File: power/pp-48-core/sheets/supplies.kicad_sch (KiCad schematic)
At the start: 24 parts, among them J4 12V AUX OUT, U1 LM5164DDA, U2 URB4812YMD-6WR3

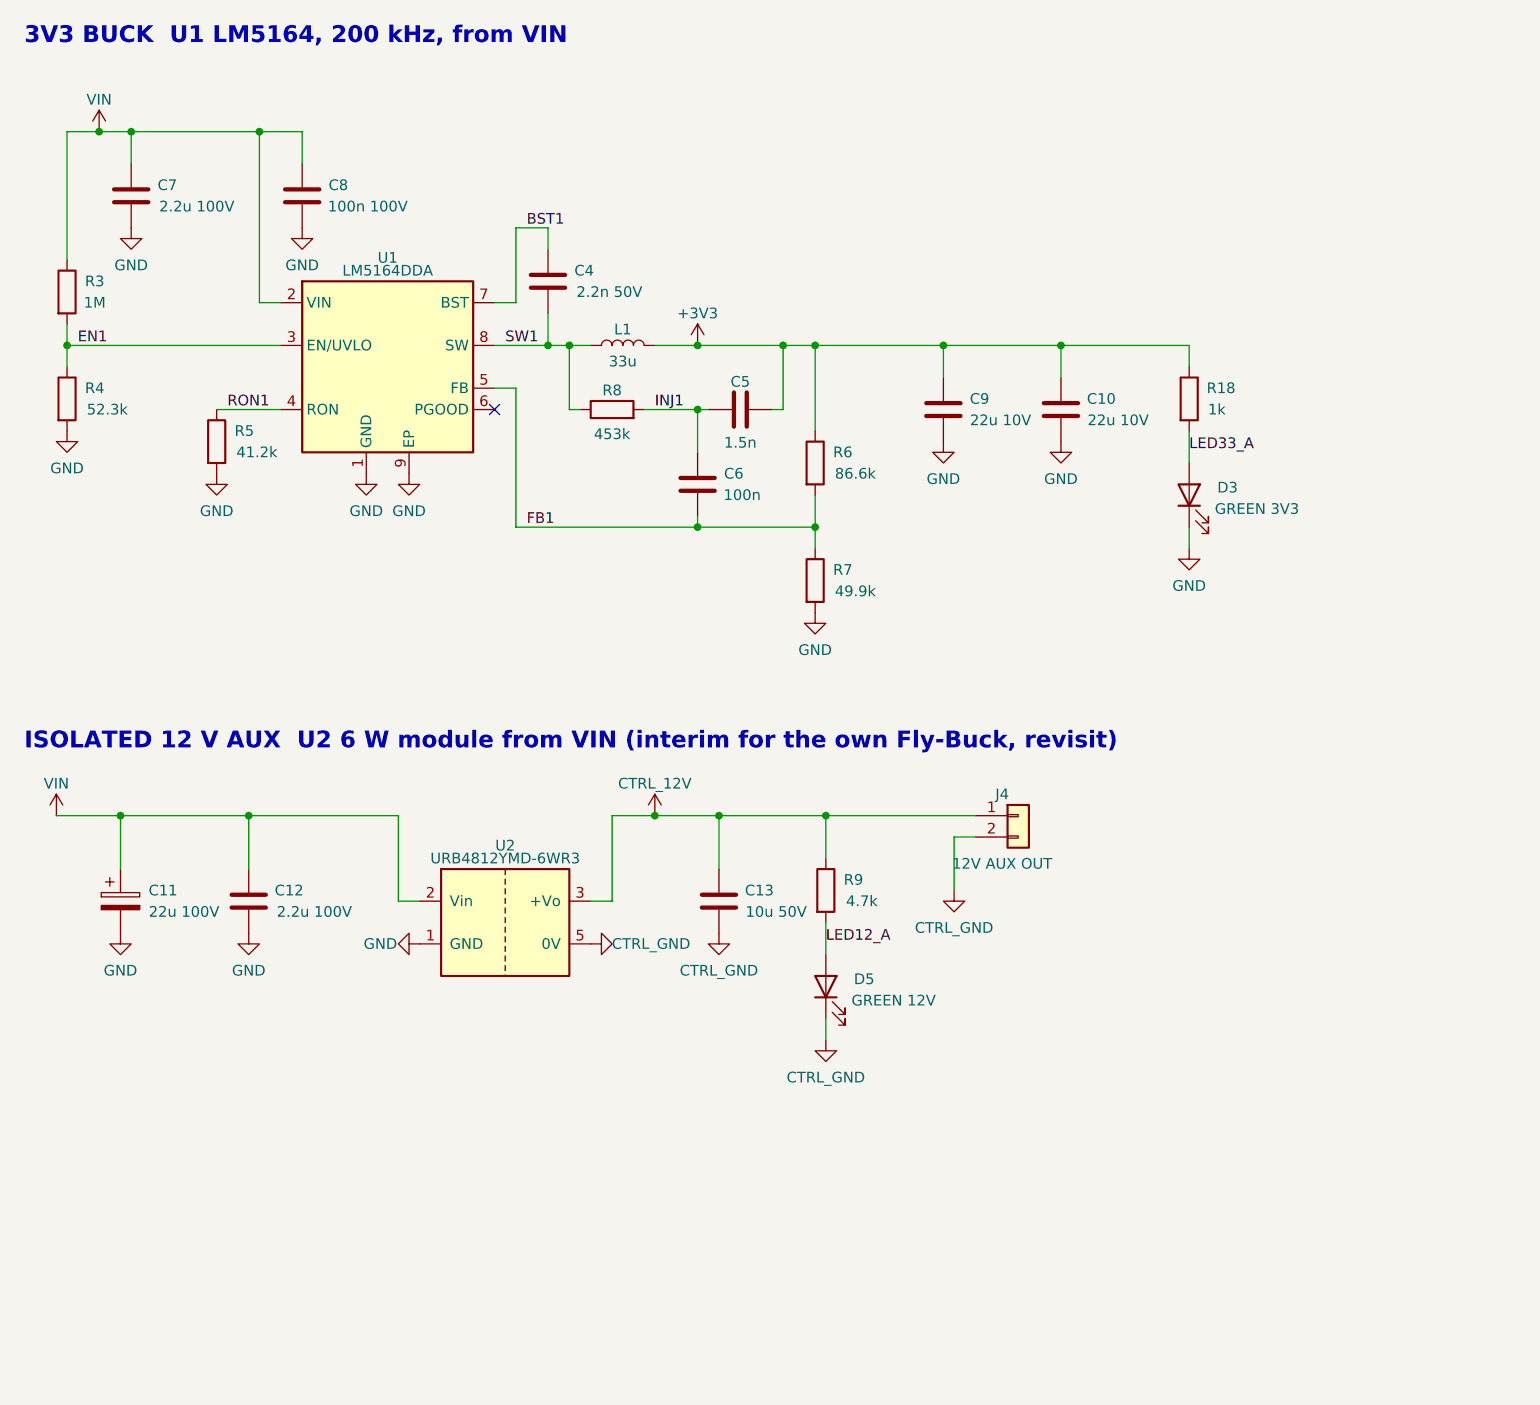
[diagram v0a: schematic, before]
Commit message: pp-48 core Supplies: LM5017 Fly-Buck replaces the interim 12 V module (ADR 0003 decision 14): L2 SRF0703-470M on the new footprint pp48:L_Bourns_SRF0703, secondary on the CTRL_GND island, PWR_FLAGs on CTRL_12V / CTRL_GND; ERC 0; handoff updated
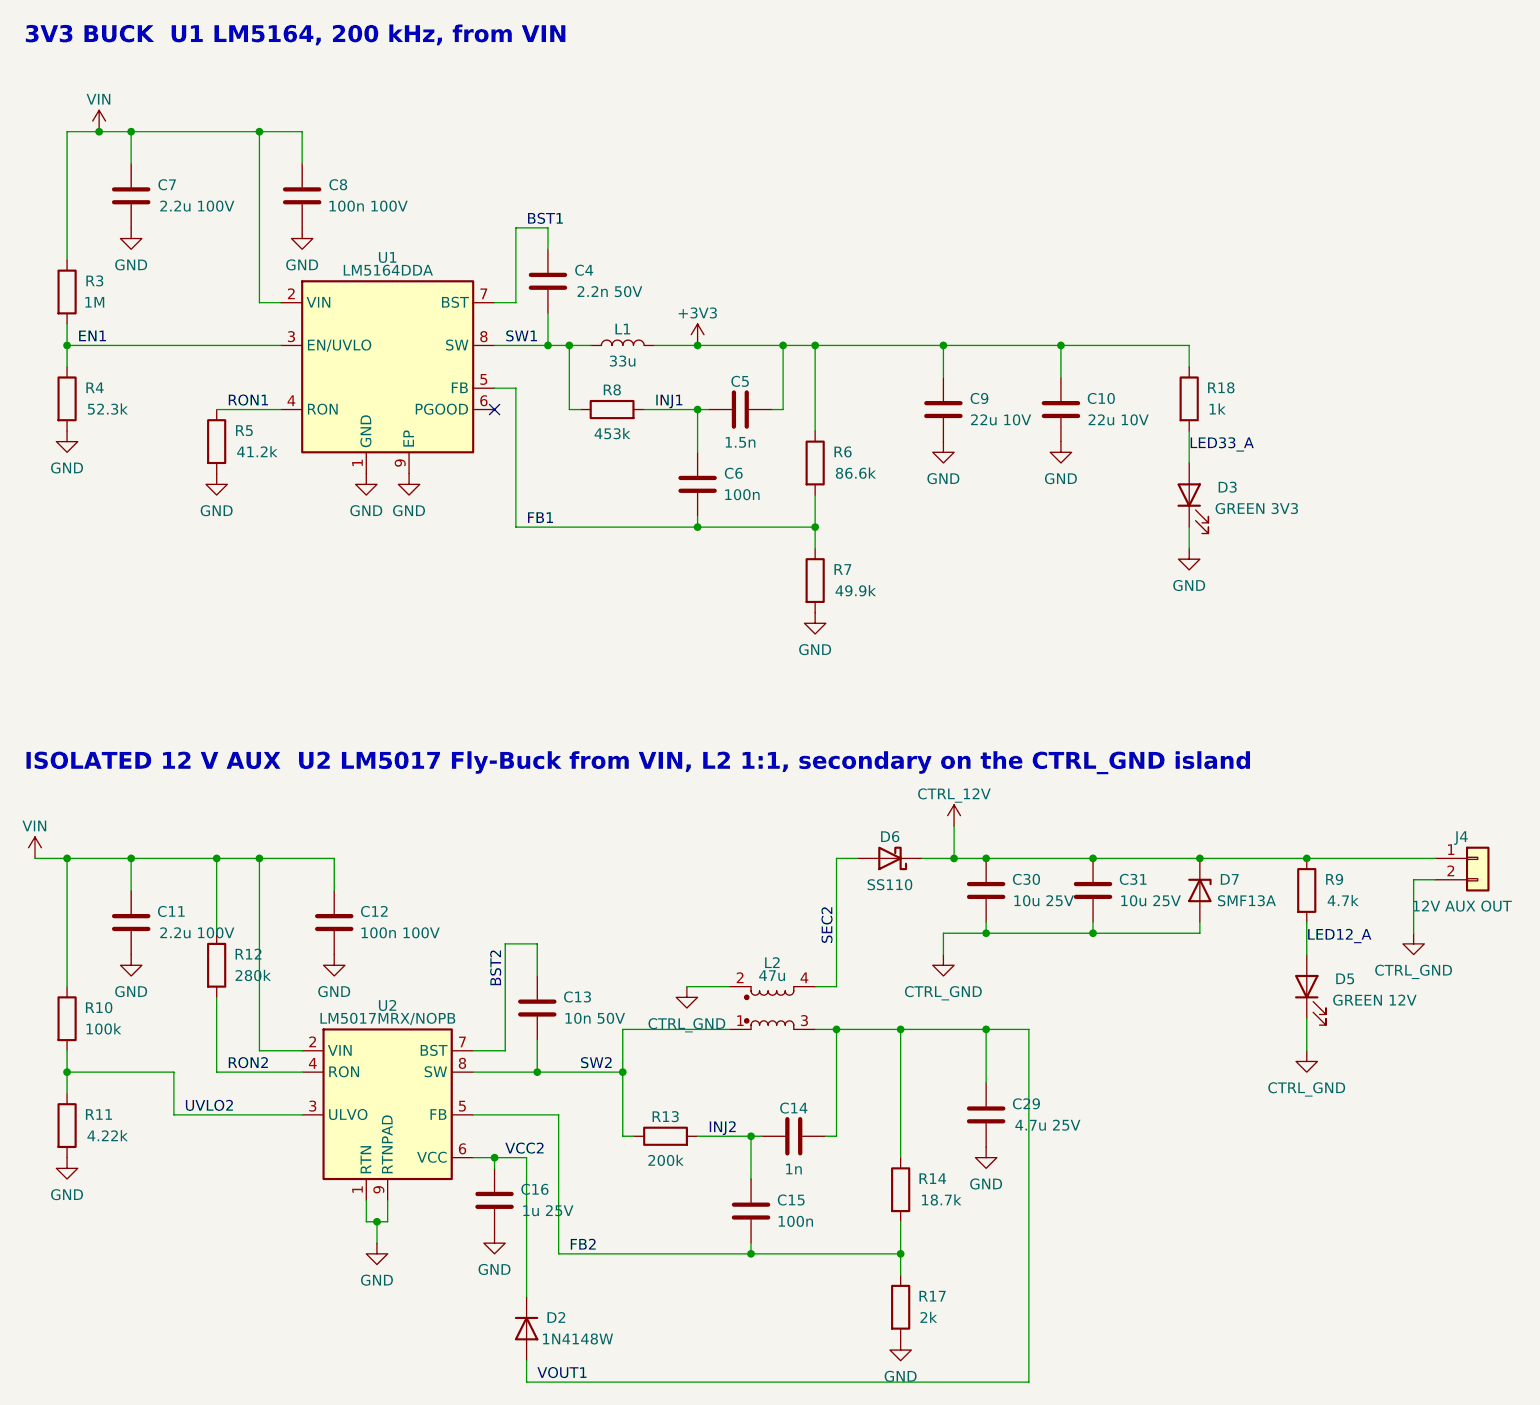
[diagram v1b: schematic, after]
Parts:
- added C14: 1n, Capacitor_SMD:C_0402_1005Metric, symbol Device:C
- added C15: 100n, Capacitor_SMD:C_0402_1005Metric, symbol Device:C
- added C16: 1u 25V, Capacitor_SMD:C_0603_1608Metric, symbol Device:C
- added C29: 4.7u 25V, Capacitor_SMD:C_0805_2012Metric, symbol Device:C
- added C30, C31: 10u 25V, Capacitor_SMD:C_0805_2012Metric, symbol Device:C
- added D2: 1N4148W, Diode_SMD:D_SOD-123, symbol Device:D
- added D6: SS110, Diode_SMD:D_SMA, symbol Device:D_Schottky
- added D7: SMF13A, Diode_SMD:D_SOD-123F, symbol Device:D_Zener
- added L2: 47u, pp48:L_Bourns_SRF0703, symbol Device:L_Coupled_1324
- added R10: 100k, Resistor_SMD:R_0805_2012Metric, symbol Device:R
- added R11: 4.22k, Resistor_SMD:R_0402_1005Metric, symbol Device:R
- added R12: 280k, Resistor_SMD:R_0805_2012Metric, symbol Device:R
- added R13: 200k, Resistor_SMD:R_0805_2012Metric, symbol Device:R
- added R14: 18.7k, Resistor_SMD:R_0402_1005Metric, symbol Device:R
- added R17: 2k, Resistor_SMD:R_0402_1005Metric, symbol Device:R
- C11: value 22u 100V -> 2.2u 100V; footprint Capacitor_SMD:CP_Elec_10x10 -> Capacitor_SMD:C_1210_3225Metric; symbol Device:C_Polarized -> Device:C; LCSC (none) -> C338133
- C12: value 2.2u 100V -> 100n 100V; footprint Capacitor_SMD:C_1210_3225Metric -> Capacitor_SMD:C_0603_1608Metric; LCSC C338133 -> (none)
- C13: value 10u 50V -> 10n 50V; footprint Capacitor_SMD:C_1210_3225Metric -> Capacitor_SMD:C_0402_1005Metric
- U2: value URB4812YMD-6WR3 -> LM5017MRX/NOPB; footprint pp48:Converter_DCDC_1x1in_THT -> Package_SO:SOIC-8-1EP_3.9x4.9mm_P1.27mm_EP2.95x4.9mm_Mask2.71x3.4mm_ThermalVias; symbol pp:DCDC_Iso_1x1_Single -> Regulator_Switching:LM5017MR; LCSC C5369743 -> C34355; MPN URB4812YMD-6WR3 (Mornsun pin-out; LCSC lists a YLPTEC part) -> (none)
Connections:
- net CTRL_12V: now also C30.1, C31.1, D6.1 (K), D7.1 (K); no longer C13.1, U2.3 (+Vo)
- net CTRL_GND: now also C30.2, C31.2, D7.2 (A), L2.2; no longer C13.2, U2.5 (0V)
- net GND: now also U2.9 (RTNPAD), C16.2, C29.2, R11.2, R17.2
- net VIN: now also R10.1, R12.1
- new net BST2: C13.1, U2.7 (BST)
- new net FB2: C15.2, R14.2, R17.1, U2.5 (FB)
- new net INJ2: C14.1, C15.1, R13.2
- new net RON2: R12.2, U2.4 (RON)
- new net SEC2: D6.2 (A), L2.4
- new net SW2: C13.2, L2.1, R13.1, U2.8 (SW)
- new net UVLO2: R10.2, R11.1, U2.3 (ULVO)
- new net VCC2: C16.1, D2.1 (K), U2.6 (VCC)
- new net VOUT1: C14.2, C29.1, D2.2 (A), L2.3, R14.1
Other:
- note added: "ISOLATED 12 V AUX U2 LM5017 Fly-Buck from VIN, L2 1:1, secondary on the CTRL_GND island"
- note removed: "ISOLATED 12 V AUX U2 6 W module from VIN (interim for the own Fly-Buck, revisit)"
- moved on the sheet: C12, C13, D5, J4, R9

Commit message: pp-48-core: GND stitch (1 via), silk (23 refs placed, 71 small ones hidden), JLC outputs; LCSC codes for the 25 passive values that had none (sch/draw.py BASIC table, JLC parts API: basic where JLC has one), copied onto the routed board; BOM 86 parts, left out only CV1/CV2, holes, J5 / JP1-3 (copper only) and DNP R28 / R29; DRC 0 unconnected, parity clean, isocheck clean
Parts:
- C10, C9: LCSC (none) -> C318780
- C12, C8: LCSC (none) -> C696916
- C13: LCSC (none) -> C15195
- C14: LCSC (none) -> C1523
- C16: LCSC (none) -> C15849
- C29: LCSC (none) -> C1779
- C30, C31: LCSC (none) -> C15850
- C4: LCSC (none) -> C1531
- C5: LCSC (none) -> C107022
- R10: LCSC (none) -> C149504
- R11: LCSC (none) -> C25898
- R12: LCSC (none) -> C5121536
- R13: LCSC (none) -> C17539
- R14: LCSC (none) -> C5153953
- R17: LCSC (none) -> C4109
- R3: LCSC (none) -> C17514
- R4: LCSC (none) -> C2998086
- R5: LCSC (none) -> C2998053
- R6: LCSC (none) -> C48533697
- R7: LCSC (none) -> C137969
- R8: LCSC (none) -> C27009
- R9: LCSC (none) -> C23162
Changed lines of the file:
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@@
 			)
 		)
-		(property "LCSC" ""
+		(property "LCSC" "C17514"
 			(at 19.05 46.99 0)
 			(hide yes)
@@
 			)
 		)
-		(property "LCSC" ""
+		(property "LCSC" "C2998086"
 			(at 19.05 59.69 0)
 			(hide yes)
@@
 			)
 		)
-		(property "LCSC" ""
+		(property "LCSC" "C2998053"
 			(at 36.83 64.77 0)
 			(hide yes)
@@
 			)
 		)
-		(property "LCSC" ""
+		(property "LCSC" "C696916"
 			(at 46.99 35.56 0)
 			(hide yes)
@@
 			)
 		)
-		(property "LCSC" ""
+		(property "LCSC" "C1531"
 			(at 76.2 45.72 0)
 			(hide yes)
@@
 			)
 		)
-		(property "LCSC" ""
+		(property "LCSC" "C27009"
 			(at 83.82 60.96 0)
 			(hide yes)
@@
 			)
 		)
-		(property "LCSC" ""
+		(property "LCSC" "C107022"
 			(at 99.06 60.96 0)
 			(hide yes)
@@
 			)
 		)
-		(property "LCSC" ""
+		(property "LCSC" "C48533697"
 			(at 107.95 67.31 0)
 			(hide yes)
@@
 			)
 		)
-		(property "LCSC" ""
+		(property "LCSC" "C137969"
 			(at 107.95 81.28 0)
 			(hide yes)
@@
 			)
 		)
-		(property "LCSC" ""
+		(property "LCSC" "C318780"
 			(at 123.19 60.96 0)
 			(hide yes)
@@
 			)
 		)
-		(property "LCSC" ""
+		(property "LCSC" "C318780"
 			(at 137.16 60.96 0)
 			(hide yes)
@@
 			)
 		)
-		(property "LCSC" ""
+		(property "LCSC" "C149504"
 			(at 19.05 133.35 0)
 			(hide yes)
@@
 			)
 		)
-		(property "LCSC" ""
+		(property "LCSC" "C25898"
 			(at 19.05 146.05 0)
 			(hide yes)
@@
 			)
 		)
-		(property "LCSC" ""
+		(property "LCSC" "C5121536"
 			(at 36.83 127 0)
 			(hide yes)
@@
 			)
 		)
-		(property "LCSC" ""
+		(property "LCSC" "C696916"
 			(at 50.8 121.92 0)
 			(hide yes)
@@
 			)
 		)
-		(property "LCSC" ""
+		(property "LCSC" "C15195"
 			(at 74.93 132.08 0)
 			(hide yes)
@@
 			)
 		)
-		(property "LCSC" ""
+		(property "LCSC" "C17539"
 			(at 90.17 147.32 0)
 			(hide yes)
@@
 			)
 		)
-		(property "LCSC" ""
+		(property "LCSC" "C1523"
 			(at 105.41 147.32 0)
 			(hide yes)
@@
 			)
 		)
-		(property "LCSC" ""
+		(property "LCSC" "C5153953"
 			(at 118.11 153.67 0)
 			(hide yes)
@@
 			)
 		)
-		(property "LCSC" ""
+		(property "LCSC" "C4109"
 			(at 118.11 167.64 0)
 			(hide yes)
@@
 			)
 		)
-		(property "LCSC" ""
+		(property "LCSC" "C15849"
 			(at 69.85 154.94 0)
 			(hide yes)
@@
 			)
 		)
-		(property "LCSC" ""
+		(property "LCSC" "C1779"
 			(at 128.27 144.78 0)
 			(hide yes)
@@
 			)
 		)
-		(property "LCSC" ""
+		(property "LCSC" "C15850"
 			(at 128.27 118.11 0)
 			(hide yes)
@@
 			)
 		)
-		(property "LCSC" ""
+		(property "LCSC" "C15850"
 			(at 140.97 118.11 0)
 			(hide yes)
@@
 			)
 		)
-		(property "LCSC" ""
+		(property "LCSC" "C23162"
 			(at 166.37 118.11 0)
 			(hide yes)

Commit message: pp-48-core 12 V aux: LM5018 + Coilcraft LPD5030V-333 replace the LM5017 + SRF0703 (ADR 0003 decision 14 revised): the SRF0703's real land pattern puts its windings' pads 0.46 mm apart with no isolation rating; the LPD5030V (4.8 x 4.8 mm, 1000 V winding to winding) has one winding per side, so the island barrier is straight (1.48 mm under the part), no pocket or vias; ~1.2 W, RON 169k (~800 kHz); footprint pp48:L_Coilcraft_LPD5030V from Coilcraft's land pattern with the LCSC 3D model; re-placed, routed, U2 exposed pad solid, gnd stitch, silk, JLC outputs. 3D models: L1 on Inductor_SMD:L_Bourns_SRR1260 (the part, SRR1260-330M; pads 0.1 mm further in than the generic 12x12, stock model), U2 on a project copy of its SOIC-8-1EP footprint pointing at the stock EP2.41x3.81 STEP (the referenced one is not shipped); both swapped on the routed board in place. ERC 0, DRC 0 unconnected, parity clean, isocheck clean, BOM 86 parts; handoff
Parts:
- L1: footprint Inductor_SMD:L_12x12mm_H6mm -> Inductor_SMD:L_Bourns_SRR1260
- L2: value 47u -> 33u; footprint pp48:L_Bourns_SRF0703 -> pp48:L_Coilcraft_LPD5030V; symbol Device:L_Coupled_1324 -> Device:L_Coupled_1243; LCSC C3273458 -> C5441621; MPN Bourns SRF0703-470M -> Coilcraft LPD5030V-333MRC
- R12: value 280k -> 169k; LCSC C5121536 -> C2933337
- U2: value LM5017MRX/NOPB -> LM5018MRX/NOPB; footprint Package_SO:SOIC-8-1EP_3.9x4.9mm_P1.27mm_EP2.95x4.9mm_Mask2.71x3.4mm_ThermalVias -> pp48:SOIC-8-1EP_3.9x4.9mm_P1.27mm_EP2.95x4.9mm_Mask2.71x3.4mm_ThermalVias; LCSC C34355 -> C471040
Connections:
- net CTRL_GND: now also L2.4; no longer L2.2
- net SEC2: now also L2.3; no longer L2.4
- net VOUT1: now also L2.2; no longer L2.3
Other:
- note added: "ISOLATED 12 V AUX U2 LM5018 Fly-Buck from VIN, L2 1:1, secondary on the CTRL_GND island"
- note removed: "ISOLATED 12 V AUX U2 LM5017 Fly-Buck from VIN, L2 1:1, secondary on the CTRL_GND island"
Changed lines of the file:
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@@
 		)
 	)
-	(text "ISOLATED 12 V AUX  U2 LM5017 Fly-Buck from VIN, L2 1:1, secondary on the CTRL_GND island"
+	(text "ISOLATED 12 V AUX  U2 LM5018 Fly-Buck from VIN, L2 1:1, secondary on the CTRL_GND island"
 		(exclude_from_sim no)
 		(at 13.97 104.14 0)
@@
 			)
 		)
-		(property "Footprint" "Inductor_SMD:L_12x12mm_H6mm"
+		(property "Footprint" "Inductor_SMD:L_Bourns_SRR1260"
 			(at 85.09 53.34 0)
 			(hide yes)
@@
 			)
 		)
-		(property "Description" "shielded, Isat >= 1.5 A, 12x12 land pattern (SRR1260 / CDRH127 class)"
+		(property "Description" "shielded, Isat >= 1.5 A, Bourns SRR1260 land pattern"
 			(at 85.09 53.34 0)
 			(hide yes)
@@
 			)
 		)
-		(property "Value" "LM5017MRX/NOPB"
+		(property "Value" "LM5018MRX/NOPB"
 			(at 57.15 133.35 0)
 			(show_name no)
@@
 			)
 		)
-		(property "Footprint" "Package_SO:SOIC-8-1EP_3.9x4.9mm_P1.27mm_EP2.95x4.9mm_Mask2.71x3.4mm_ThermalVias"
+		(property "Footprint" "pp48:SOIC-8-1EP_3.9x4.9mm_P1.27mm_EP2.95x4.9mm_Mask2.71x3.4mm_ThermalVias"
 			(at 57.15 142.24 0)
 			(hide yes)
@@
 			)
 		)
-		(property "Description" "100 V 600 mA COT synchronous buck, Fly-Buck primary 12.7 V"
+		(property "Description" "100 V 300 mA COT synchronous buck (LM5017 pinout), Fly-Buck primary 12.7 V"
 			(at 57.15 142.24 0)
 			(hide yes)
@@
 			)
 		)
-		(property "LCSC" "C34355"
+		(property "LCSC" "C471040"
 			(at 57.15 142.24 0)
 			(hide yes)
@@
 			)
 		)
-		(property "Value" "280k"
+		(property "Value" "169k"
 			(at 41.116 128.27 0)
 			(show_name no)
@@
 			)
 		)
-		(property "Description" "RON from VIN: fsw = VOUT1 / (9e-11 x RON) ~ 500 kHz"
+		(property "Description" "RON from VIN: fsw = VOUT1 / (9e-11 x RON) ~ 800 kHz, on-time 200 ns at 75 V"
 			(at 36.83 127 0)
 			(hide yes)
@@
 			)
 		)
-		(property "LCSC" "C5121536"
+		(property "LCSC" "C2933337"
 			(at 36.83 127 0)
 			(hide yes)
@@
 	)
 	(symbol
-		(lib_id "Device:L_Coupled_1324")
+		(lib_id "Device:L_Coupled_1243")
 		(at 102.87 132.08 0)
 		(mirror x)
@@
 			)
 		)
-		(property "Value" "47u"
+		(property "Value" "33u"
 			(at 102.87 128.27 0)
 			(show_name no)
@@
 			)
 		)
-		(property "Footprint" "pp48:L_Bourns_SRF0703"
+		(property "Footprint" "pp48:L_Coilcraft_LPD5030V"
 			(at 102.87 132.08 0)
 			(hide yes)
@@
 			)
 		)
-		(property "Description" "Fly-Buck coupled inductor 1:1, 47 uH, Isat 1.14 A, hi-pot 500 Vrms; N1 1-3 primary, N2 2-4 secondary (dots 1, 2)"
+		(property "Description" "Fly-Buck coupled inductor 1:1, 33 uH, Isat 0.49 A (10 %), 1000 V winding to winding; L1 1-2 primary, L2 4-3 secondary (dots 1, 4)"
 			(at 102.87 132.08 0)
 			(hide yes)
@@
 			)
 		)
-		(property "LCSC" "C3273458"
+		(property "LCSC" "C5441621"
 			(at 102.87 132.08 0)
 			(hide yes)
@@
 			)
 		)
-		(property "MPN" "Bourns SRF0703-470M"
+		(property "MPN" "Coilcraft LPD5030V-333MRC"
 			(at 102.87 132.08 0)
 			(hide yes)
